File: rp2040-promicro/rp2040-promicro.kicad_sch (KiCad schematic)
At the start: 31 parts, among them J1 USB2.0_C_v3, J2 ProMicro-LeftPin, J3 ProMicro-RightPin, SW1 SW_Push, U1 RP2040, U2 W25Q128JVS, U3 AZ1117-3.3, Y1 Crystal_GND24

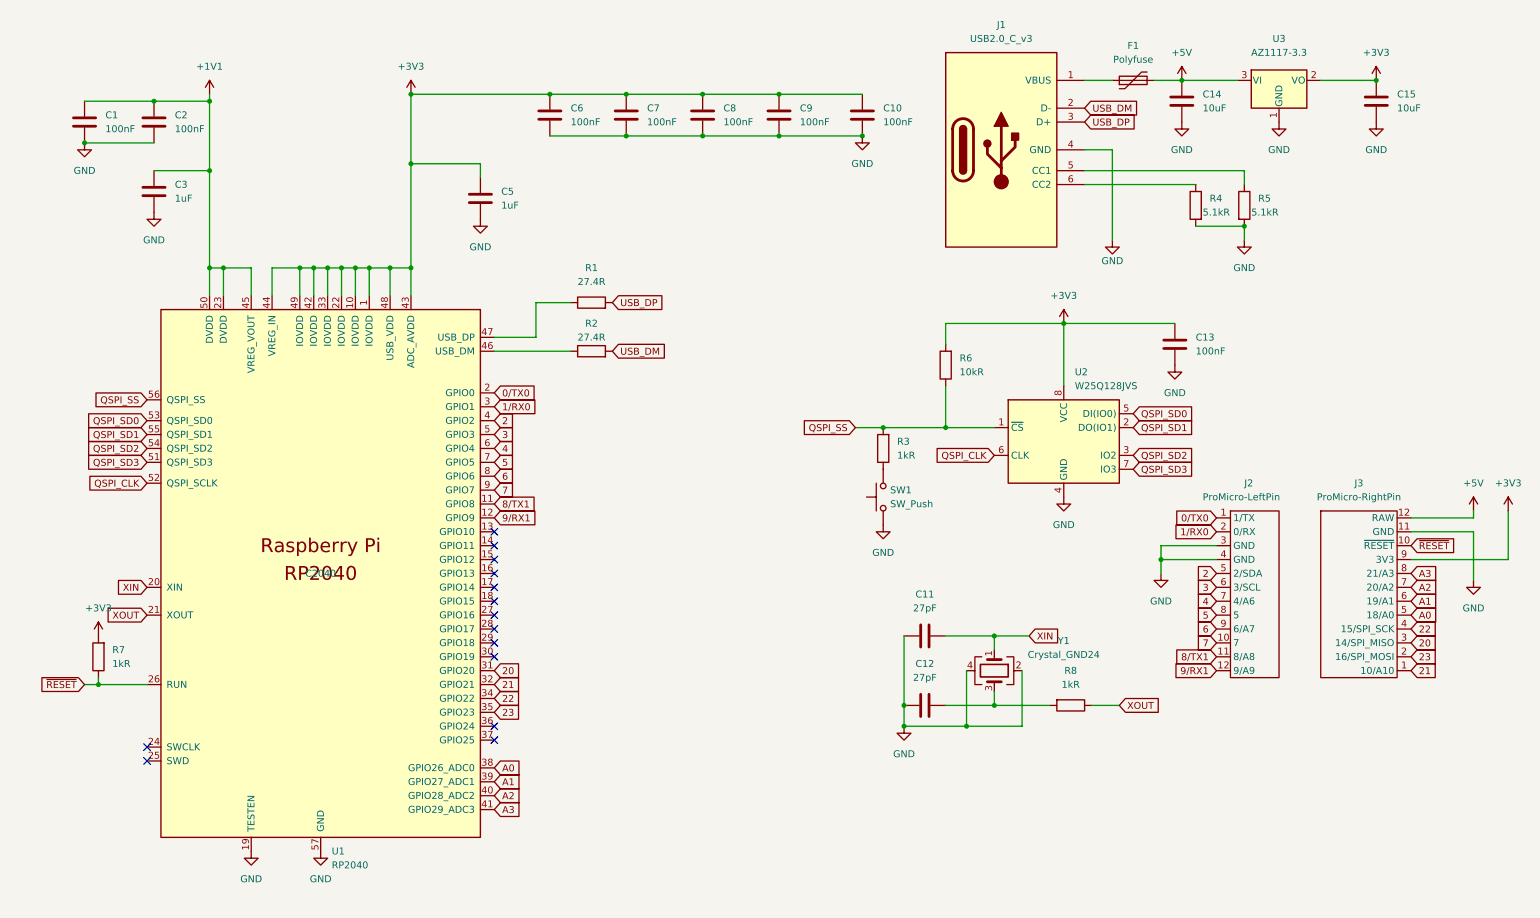
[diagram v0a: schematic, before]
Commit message: v2.0.1で最後に位置を整列したのが未コミットだった
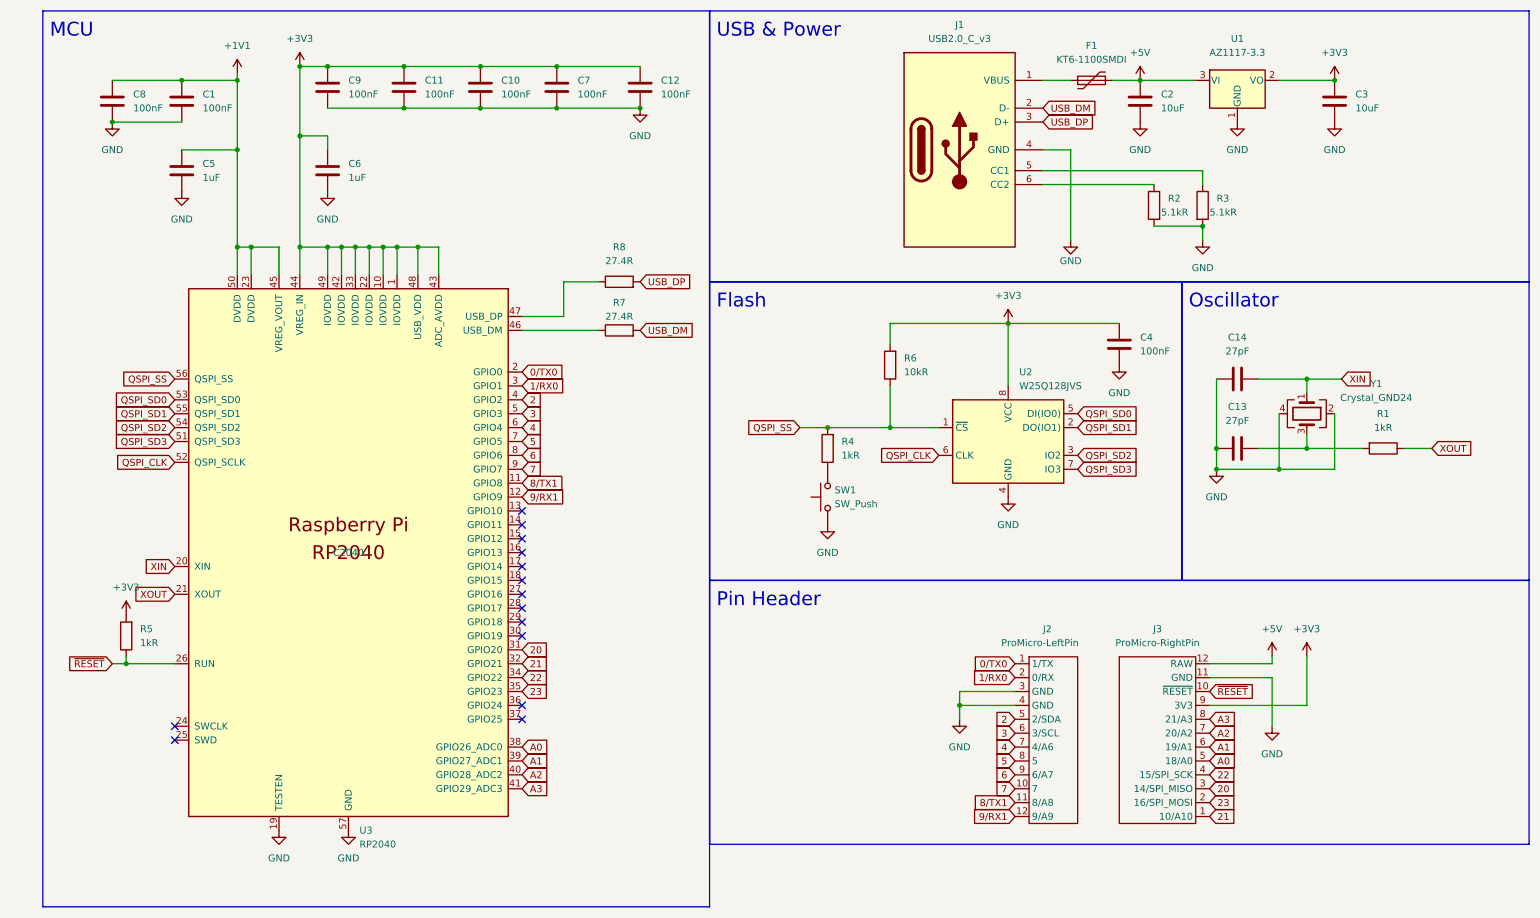
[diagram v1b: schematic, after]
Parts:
- F1: value Polyfuse -> KT6-1100SMDI
- renumbered C2 to C1, C8 to C10, C7 to C11, C10 to C12, C12 to C13, C11 to C14, C14 to C2, C15 to C3, C13 to C4, C3 to C5, C5 to C6, C9 to C7, C1 to C8, C6 to C9, R8 to R1, R4 to R2, R5 to R3, R3 to R4, R7 to R5, R2 to R7, R1 to R8, U3 to U1, U1 to U3
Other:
- note added: "Flash"
- note added: "MCU"
- note added: "Oscillator"
- note added: "Pin Header"
- note added: "USB & Power"
- moved on the sheet: C1, C10, C11, C12, C13, C14, C2, C3, C4, C5, C6, C7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
